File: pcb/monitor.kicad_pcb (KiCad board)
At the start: 4 copper layers, 100 x 100 mm, 146 parts, among them K101 DG128-02P, K102 DG128-02P, K103 DG128-02P, K104 DG128-02P, K105 DG128-02P, K106 DG128-02P, K107 DG128-02P, K108 DG128-02P, K109 DG128-02P, K110 DG128-02P, K111 DG128-02P, K112 DG128-02P, K113 JUMPER_3, K114 JUMPER_3, K115 MOUNT, K116 MOUNT, K117 MOUNT, K118 MOUNT, K119 MOUNT, K120 CONNECT_4, K121 CONNECT_4, K122 MOUNT, K401 CONNECT_6, K7 DG128-02P, K8 DG128-02P, T201 ZUMT718, T202 ZUMT718, T203 ZUMT718, T204 ZUMT718, T205 ZUMT718, T206 ZUMT718, T207 ZUMT718, T208 ZUMT718, T209 ZUMT718, T210 ZUMT718, T211 ZUMT718, T212 ZUMT718, U1 LTC6803-3, U401 ADUM5401

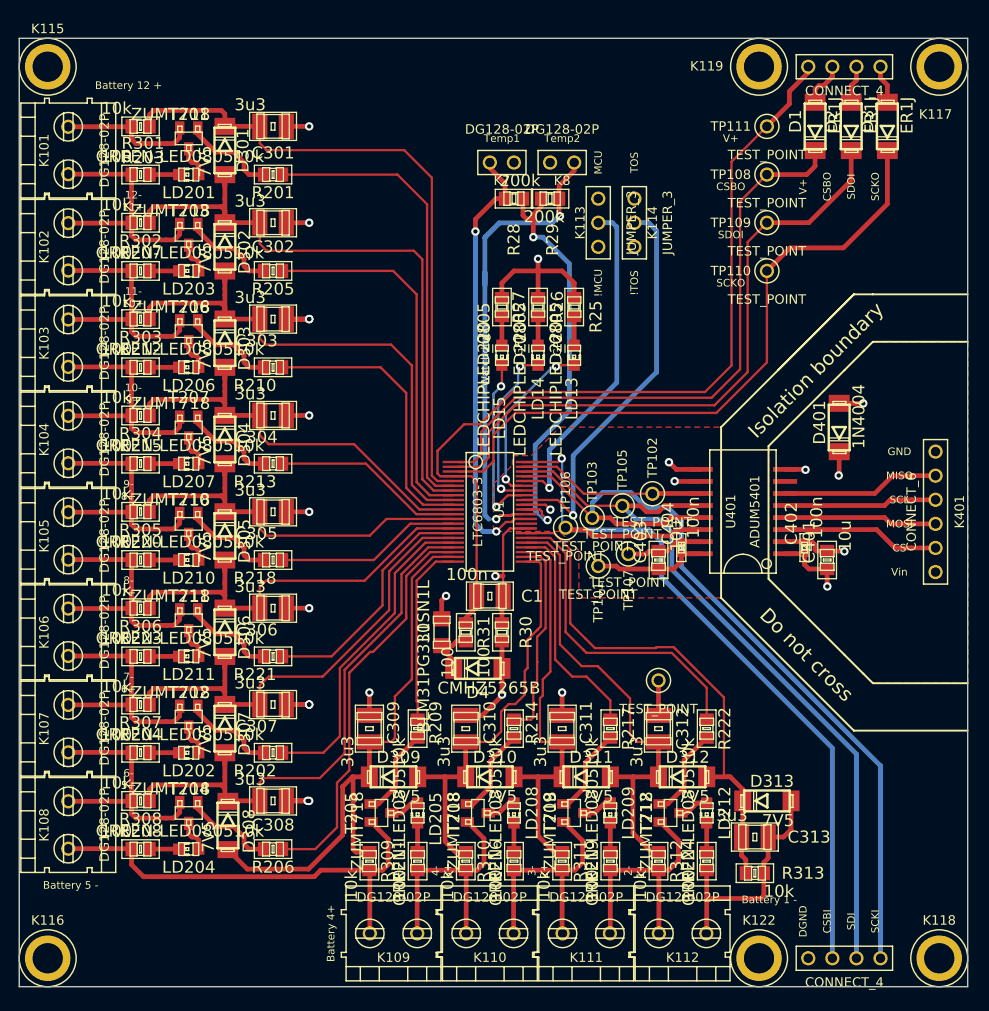
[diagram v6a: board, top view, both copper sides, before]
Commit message: Add logos
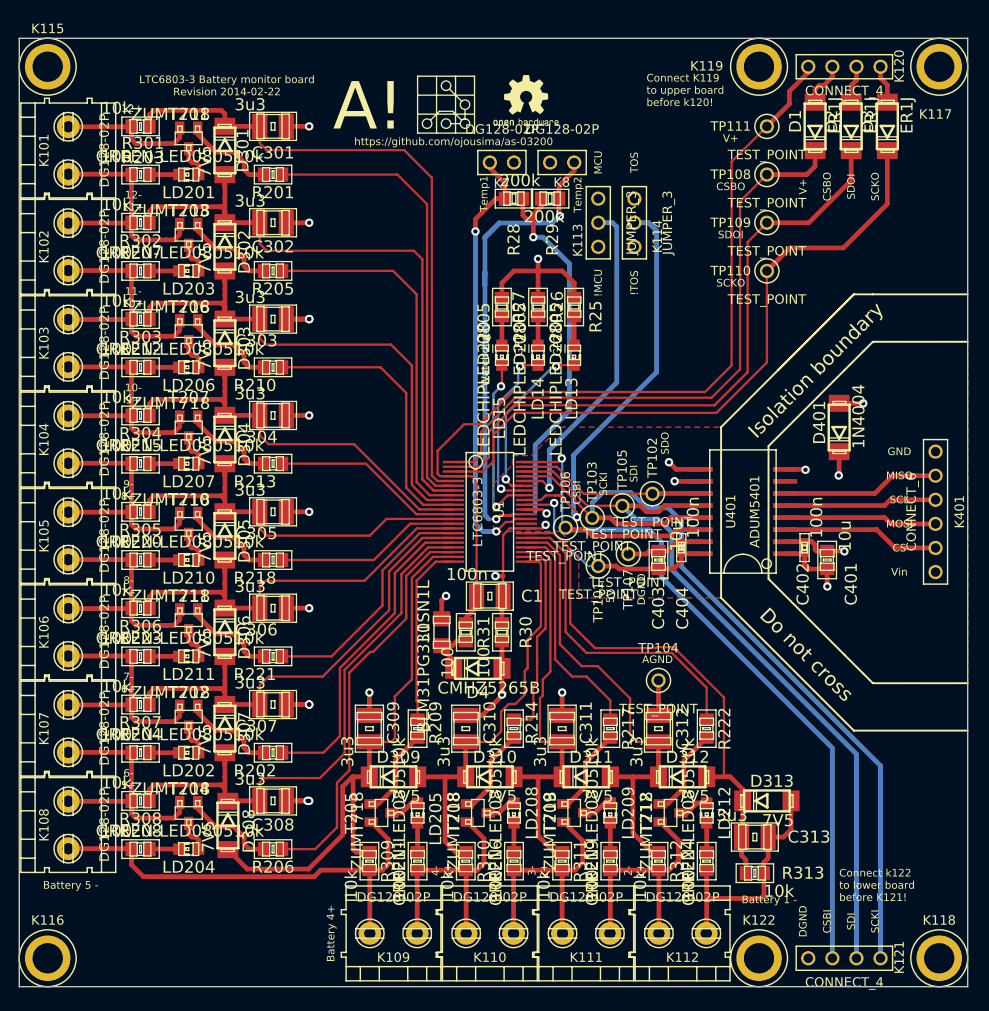
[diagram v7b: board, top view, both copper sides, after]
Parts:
- added G***: LOGO, logos:OSHWLOGO0.3IN, F.Cu at (134.6, 27.9)
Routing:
- net /Isolation/5V: track 34.1 -> 43.1 mm
- net DGND: track 25.6 -> 27.8 mm, vias 2 -> 3
- net /Vref: track 46.7 -> 45.6 mm
- net /TOS: track 42.4 -> 43.5 mm
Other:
- board text added: "12+"
- board text added: "5V"
- board text added: "A!"
- board text added: "AGND"
- board text added: "Connect K119 to upper board before k120!"
- board text added: "Connect k122 to lower board before K121!"
- board text added: "LTC6803-3 Battery monitor board Revision 2014-02-22"
- board text added: "SDO"
- board text added: "https://github.com/ojousima/as-03200"
- board text removed: "Battery 12 +"

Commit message: First production version
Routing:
- net /discharge/BATT12+: track 30.2 -> 32.1 mm
- net /V+: track 91.9 -> 93.2 mm
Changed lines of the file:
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@@
     (thickness 1.6)
     (drawings 141)
-    (tracks 1001)
+    (tracks 1003)
     (zones 0)
     (modules 147)
@@
     (15 F.Cu signal)
     (2 Inner2.Cu power hide)
-    (1 Inner1.Cu power hide)
+    (1 Inner1.Cu power)
     (0 B.Cu jumper)
     (16 B.Adhes user)
@@
   )
   (setup
-    (last_trace_width 0.245)
+    (last_trace_width 0.5)
     (user_trace_width 0.245)
     (user_trace_width 0.25)
@@
   (segment (start 143.4 69) (end 143.45 68.95) (width 0.5) (layer B.Cu) (net 41))
   (segment (start 143.45 68.95) (end 152.2 60.2) (width 0.5) (layer B.Cu) (net 41))
+  (segment (start 168.19 28) (end 168.19 29.11) (width 0.5) (layer F.Cu) (net 42))
+  (segment (start 166.11 34.29) (end 163.83 34.29) (width 0.5) (layer F.Cu) (net 42))
+  (segment (start 167.2 33.2) (end 166.11 34.29) (width 0.5) (layer F.Cu) (net 42))
+  (segment (start 167.2 30.1) (end 167.2 33.2) (width 0.5) (layer F.Cu) (net 42))
+  (segment (start 168.19 29.11) (end 167.2 30.1) (width 0.5) (layer F.Cu) (net 42))
   (segment (start 133.22046 83.82) (end 133.22046 71.72046) (width 0.245) (layer F.Cu) (net 42))
   (segment (start 132.68 71.18) (end 130.77 71.18) (width 0.245) (layer F.Cu) (net 42))
@@
   (segment (start 160.1 59.5) (end 160.1 38.02) (width 0.245) (layer F.Cu) (net 42))
   (segment (start 160.1 38.02) (end 163.83 34.29) (width 0.245) (layer F.Cu) (net 42))
-  (segment (start 168.19 28) (end 168.19 28.61) (width 0.5) (layer F.Cu) (net 42))
-  (segment (start 168.19 28.61) (end 166.2 30.6) (width 0.5) (layer F.Cu) (net 42))
-  (segment (start 166.2 30.6) (end 166.2 31.92) (width 0.5) (layer F.Cu) (net 42))
-  (segment (start 166.2 31.92) (end 163.83 34.29) (width 0.5) (layer F.Cu) (net 42))
   (segment (start 133.22046 83.82) (end 133.22046 84.97954) (width 0.5) (layer F.Cu) (net 42))
   (segment (start 132.08 86.12) (end 132.08 86.68004) (width 0.5) (layer F.Cu) (net 42))
@@
   (via (at 135.3 74.4) (size 0.889) (layers F.Cu B.Cu) (net 47))
   (segment (start 136.52 73.18) (end 135.3 74.4) (width 0.245) (layer F.Cu) (net 47))
-  (segment (start 159.1 28) (end 163 28) (width 1.5) (layer Inner1.Cu) (net 48))
   (segment (start 163 28) (end 163.2 28) (width 1.5) (layer Inner1.Cu) (net 48))
-  (segment (start 163.2 28) (end 166.5 31.3) (width 1.5) (layer Inner1.Cu) (net 48))
+  (segment (start 163.2 28) (end 165.4 30.2) (width 1.5) (layer Inner1.Cu) (net 48))
   (segment (start 163 28) (end 162.9 28) (width 1.5) (layer Inner1.Cu) (net 48))
-  (segment (start 162.9 28) (end 160.1 30.8) (width 1.5) (layer Inner1.Cu) (net 48))
+  (segment (start 162.9 28) (end 159.7 31.2) (width 1.5) (layer Inner1.Cu) (net 48))
+  (segment (start 163 28) (end 156.4 28) (width 1.5) (layer Inner1.Cu) (net 48))
+  (segment (start 156.4 28) (end 156.3 27.9) (width 1.5) (layer Inner1.Cu) (net 48))
   (segment (start 129.54 86.21014) (end 129.54 84.26) (width 0.5) (layer F.Cu) (net 48))
   (segment (start 129.54 84.26) (end 130 83.8) (width 0.5) (layer F.Cu) (net 48))
@@
     (polygon
       (pts
-        (xy 85 25) (xy 185 25) (xy 185 52) (xy 173 52) (xy 161 52)
-        (xy 159 51) (xy 159 33) (xy 134 33) (xy 131 36) (xy 131 84)
-        (xy 131 96) (xy 128 99) (xy 85 99)
+        (xy 85 25) (xy 166.3 25) (xy 166.1 31.1) (xy 164.3 31.1) (xy 159.1 32.9)
+        (xy 159 33) (xy 134 33) (xy 131 36) (xy 131 84) (xy 131 96)
+        (xy 128 99) (xy 85 99)
       )
     )
@@
     )
   )
-  (zone (net 61) (net_name AGND) (layer Inner2.Cu) (hatch edge 0.508)
-    (connect_pads (clearance 1))
-    (min_thickness 0.254)
-    (fill (arc_segments 16) (thermal_gap 0.508) (thermal_bridge_width 0.508))
-    (polygon
-      (pts
-        (xy 185 32) (xy 175 32) (xy 174 33) (xy 134 33) (xy 131 36)
-        (xy 131 88) (xy 138.6 88) (xy 138.6 78.2) (xy 141.6 78.2) (xy 142.6 79.4)
-        (xy 142.6 86) (xy 151 86) (xy 161 96) (xy 161 98.4) (xy 168.2 104.4)
-        (xy 168.2 116) (xy 165.8 118.4) (xy 165.8 125) (xy 85 125) (xy 85 25)
-        (xy 185 25)
-      )
-    )
-  )
   (zone (net 62) (net_name DGND) (layer Inner2.Cu) (hatch edge 0.508)
     (connect_pads (clearance 0.254))
@@
         (xy 169.8 101.4) (xy 152 84) (xy 144 84) (xy 144 79) (xy 142 77)
         (xy 137 77) (xy 137 86) (xy 133 86) (xy 133 38) (xy 135 36)
-        (xy 174 36) (xy 176 34) (xy 185 34) (xy 185 52) (xy 173 52)
-        (xy 159 66) (xy 159 84) (xy 173 98) (xy 185 98)
+        (xy 162.5 36) (xy 162.5 34) (xy 163.6 33.1) (xy 166.6 33) (xy 166.8 25)
+        (xy 185 25) (xy 185 52) (xy 173 52) (xy 159 66) (xy 159 84)
+        (xy 173 98) (xy 185 98)
       )
     )
@@
       )
     )
+  )
+  (zone (net 61) (net_name AGND) (layer Inner2.Cu) (hatch edge 0.508)
+    (connect_pads (clearance 0.254))
+    (min_thickness 0.254)
+    (fill (arc_segments 16) (thermal_gap 0.508) (thermal_bridge_width 0.508))
+    (polygon
+      (pts
+        (xy 165.9 25) (xy 165.8 31.4) (xy 164.1 31.4) (xy 161.7 33) (xy 134 33)
+        (xy 131 36) (xy 131 88) (xy 138.6 88) (xy 138.6 78.2) (xy 141.6 78.2)
+        (xy 142.6 79.4) (xy 142.6 86) (xy 151 86) (xy 161 96) (xy 161 98.4)
+        (xy 168.2 104.4) (xy 168.2 116) (xy 165.8 118.4) (xy 165.8 125) (xy 85 125)
+        (xy 85 25)
+      )
+    )
